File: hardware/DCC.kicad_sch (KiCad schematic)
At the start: 5 parts, among them U1001 6N137

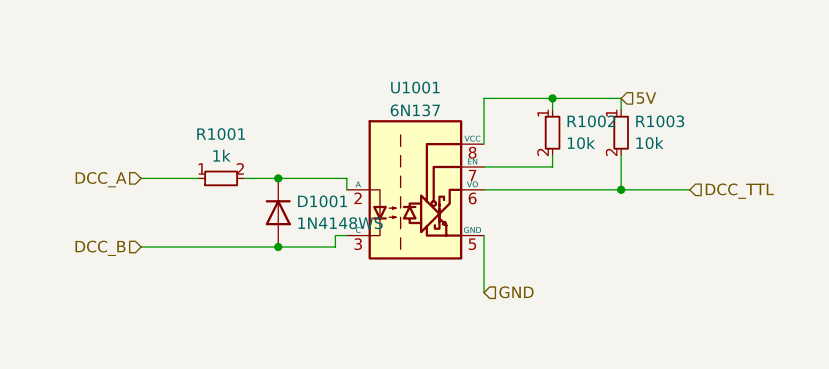
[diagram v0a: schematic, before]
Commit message: update board file, made similar to OS solenoid decoder
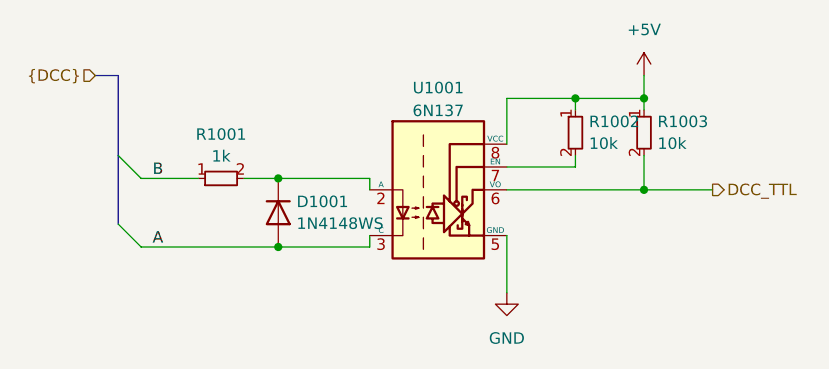
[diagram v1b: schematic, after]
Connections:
- net 5V renamed +5V
- net DCC_A renamed B
- net DCC_B renamed A
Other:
- moved on the sheet: R1002, R1003, U1001
